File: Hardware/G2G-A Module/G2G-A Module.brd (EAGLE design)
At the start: 13.1 x 12.8 mm, 4 parts, among them J1 GROVE-4P-2.0-3470130P1

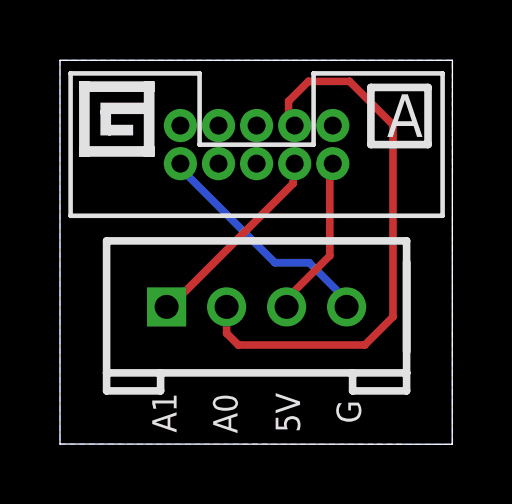
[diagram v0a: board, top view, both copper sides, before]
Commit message: Rotated the G plug 180 degrees.
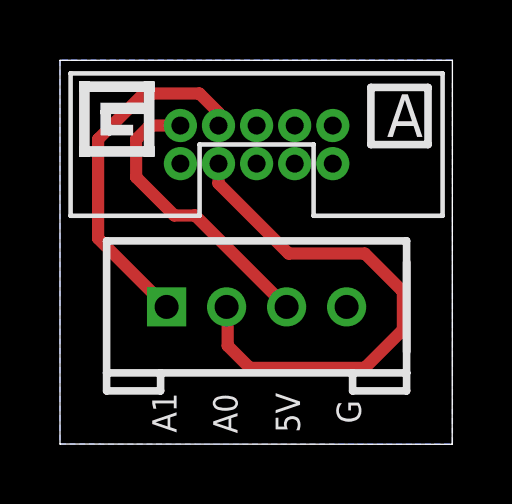
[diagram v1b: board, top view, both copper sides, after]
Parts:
- turned U$1 to 180 degrees
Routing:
- net GND: track 7.74 -> 0.00 mm
- net A1: track 6.59 -> 11.9 mm
- net +5V: track 5.39 -> 9.73 mm
- net A0: track 18.6 -> 17.6 mm
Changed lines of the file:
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@@
 <element name="J1" library="SoftDust" package="4P-2.0" value="GROVE-4P-2.0-3470130P1" x="6.5532" y="4.572" smashed="yes"/>
 <element name="LOGO1" library="SparkFun-Aesthetics" package="OSHW-LOGO-S" value="OSHW-LOGOS" x="1.8796" y="1.778" rot="MR0"/>
-<element name="U$1" library="SoftDust" package="2X5_1.27MM_FEMALE_PLUG" value="2X5_1.27MM_FEMALE_PLUG" x="6.5532" y="9.9822" rot="MR0"/>
+<element name="U$1" library="SoftDust" package="2X5_1.27MM_FEMALE_PLUG" value="2X5_1.27MM_FEMALE_PLUG" x="6.5532" y="9.9822" rot="MR180"/>
 <element name="FRAME1" library="SparkFun-Aesthetics" package="DUMMY" value="" x="0" y="-1.27">
 <attribute name="VERSION" value="v1.0" x="0" y="-1.27" size="1.778" layer="27" display="off"/>
@@
 <contactref element="U$1" pad="10"/>
 <contactref element="J1" pad="4"/>
-<wire x1="4.191" y1="9.017" x2="4.191" y2="9.2456" width="0.254" layer="16"/>
-<wire x1="7.1628" y1="6.0452" x2="4.191" y2="9.017" width="0.254" layer="16"/>
-<wire x1="8.3058" y1="6.0452" x2="7.1628" y2="6.0452" width="0.254" layer="16"/>
-<wire x1="9.4488" y1="4.9022" x2="8.3058" y2="6.0452" width="0.254" layer="16"/>
-<wire x1="4.191" y1="9.2456" x2="4.0132" y2="9.3472" width="0.254" layer="16"/>
-<wire x1="9.4488" y1="4.9022" x2="9.5532" y2="4.572" width="0.254" layer="16"/>
 <polygon width="0.254" layer="16" isolate="0.4064">
 <vertex x="0" y="0"/>
@@
 <contactref element="J1" pad="3"/>
 <contactref element="U$1" pad="2"/>
-<wire x1="8.9916" y1="6.2738" x2="8.9916" y2="9.2456" width="0.254" layer="1"/>
-<wire x1="7.62" y1="4.9022" x2="8.9916" y2="6.2738" width="0.254" layer="1"/>
-<wire x1="8.9916" y1="9.2456" x2="9.0932" y2="9.3472" width="0.254" layer="1"/>
-<wire x1="7.62" y1="4.9022" x2="7.5532" y2="4.572" width="0.254" layer="1"/>
+<wire x1="7.5532" y1="4.572" x2="4.5052" y2="7.62" width="0.4064" layer="1"/>
+<wire x1="4.5052" y1="7.62" x2="3.81" y2="7.62" width="0.4064" layer="1"/>
+<wire x1="3.81" y1="7.62" x2="2.54" y2="8.89" width="0.4064" layer="1"/>
+<wire x1="2.54" y1="8.89" x2="2.54" y2="10.16" width="0.4064" layer="1"/>
+<wire x1="2.54" y1="10.16" x2="2.9972" y2="10.6172" width="0.4064" layer="1"/>
+<wire x1="2.9972" y1="10.6172" x2="4.0132" y2="10.6172" width="0.4064" layer="1"/>
 </signal>
 <signal name="A0">
 <contactref element="J1" pad="2"/>
 <contactref element="U$1" pad="3"/>
-<wire x1="5.5532" y1="4.572" x2="5.5532" y2="3.6924" width="0.254" layer="1"/>
-<wire x1="5.5532" y1="3.6924" x2="5.9436" y2="3.302" width="0.254" layer="1"/>
-<wire x1="5.9436" y1="3.302" x2="10.16" y2="3.302" width="0.254" layer="1"/>
-<wire x1="10.16" y1="3.302" x2="11.0998" y2="4.2418" width="0.254" layer="1"/>
-<wire x1="11.0998" y1="4.2418" x2="11.0998" y2="10.6426" width="0.254" layer="1"/>
-<wire x1="11.0998" y1="10.6426" x2="9.652" y2="12.0904" width="0.254" layer="1"/>
-<wire x1="9.652" y1="12.0904" x2="8.2804" y2="12.0904" width="0.254" layer="1"/>
-<wire x1="8.2804" y1="12.0904" x2="7.62" y2="11.43" width="0.254" layer="1"/>
-<wire x1="7.62" y1="11.43" x2="7.62" y2="10.8204" width="0.254" layer="1"/>
-<wire x1="7.62" y1="10.8204" x2="7.8232" y2="10.6172" width="0.254" layer="1"/>
+<wire x1="5.5532" y1="4.572" x2="5.588" y2="4.5372" width="0.4064" layer="1"/>
+<wire x1="5.588" y1="4.5372" x2="5.588" y2="3.2766" width="0.4064" layer="1"/>
+<wire x1="5.588" y1="3.2766" x2="6.3246" y2="2.54" width="0.4064" layer="1"/>
+<wire x1="6.3246" y1="2.54" x2="10.16" y2="2.54" width="0.4064" layer="1"/>
+<wire x1="10.16" y1="2.54" x2="11.43" y2="3.81" width="0.4064" layer="1"/>
+<wire x1="11.43" y1="3.81" x2="11.43" y2="5.08" width="0.4064" layer="1"/>
+<wire x1="11.43" y1="5.08" x2="10.16" y2="6.35" width="0.4064" layer="1"/>
+<wire x1="10.16" y1="6.35" x2="7.62" y2="6.35" width="0.4064" layer="1"/>
+<wire x1="7.62" y1="6.35" x2="5.2832" y2="8.6868" width="0.4064" layer="1"/>
+<wire x1="5.2832" y1="8.6868" x2="5.2832" y2="9.3472" width="0.4064" layer="1"/>
 </signal>
 <signal name="A1">
 <contactref element="J1" pad="1"/>
 <contactref element="U$1" pad="4"/>
-<wire x1="7.7724" y1="8.6868" x2="7.7724" y2="9.144" width="0.254" layer="1"/>
-<wire x1="3.6576" y1="4.572" x2="7.7724" y2="8.6868" width="0.254" layer="1"/>
-<wire x1="7.7724" y1="9.144" x2="7.8232" y2="9.3472" width="0.254" layer="1"/>
-<wire x1="3.6576" y1="4.572" x2="3.5532" y2="4.572" width="0.254" layer="1"/>
+<wire x1="3.5532" y1="4.572" x2="1.27" y2="6.8552" width="0.4064" layer="1"/>
+<wire x1="1.27" y1="6.8552" x2="1.27" y2="10.16" width="0.4064" layer="1"/>
+<wire x1="1.27" y1="10.16" x2="2.794" y2="11.684" width="0.4064" layer="1"/>
+<wire x1="2.794" y1="11.684" x2="4.6482" y2="11.684" width="0.4064" layer="1"/>
+<wire x1="4.6482" y1="11.684" x2="5.2832" y2="11.049" width="0.4064" layer="1"/>
+<wire x1="5.2832" y1="11.049" x2="5.2832" y2="10.6172" width="0.4064" layer="1"/>
 </signal>
 </signals>

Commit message: Replaced all 'G' logos with a new part for the logo.
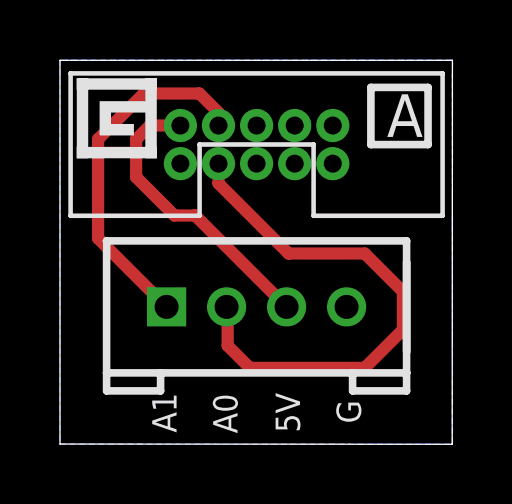
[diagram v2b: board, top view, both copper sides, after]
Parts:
- added U$2: GADGETEER_LOGO_SMALL, SoftDust:GADGETEER_LOGO_SMALL
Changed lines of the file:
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@@
 <setting verticaltext="up"/>
 </settings>
-<grid distance="0.05" unitdist="inch" unit="mm" style="lines" multiple="1" display="no" altdistance="0.0254" altunitdist="mm" altunit="mm"/>
+<grid distance="1.27" unitdist="mm" unit="mm" style="lines" multiple="1" display="yes" altdistance="0.0254" altunitdist="mm" altunit="mm"/>
 <layers>
 <layer number="1" name="Top" color="4" fill="1" visible="yes" active="yes"/>
@@
 <text x="5.9182" y="0.3556" size="0.8128" layer="21" font="vector" rot="R90">A0</text>
 <text x="3.8862" y="0.381" size="0.8128" layer="21" font="vector" rot="R90">A1</text>
-<rectangle x1="0.635" y1="9.5758" x2="3.1496" y2="9.9314" layer="21"/>
-<rectangle x1="0.635" y1="11.7348" x2="3.1496" y2="12.0904" layer="21"/>
-<rectangle x1="1.7145" y1="10.6553" x2="4.2291" y2="11.0109" layer="21" rot="R90"/>
-<rectangle x1="-0.4445" y1="10.6553" x2="2.0701" y2="11.0109" layer="21" rot="R90"/>
-<rectangle x1="1.3462" y1="10.9982" x2="2.8194" y2="11.3792" layer="21"/>
-<rectangle x1="1.3462" y1="10.287" x2="1.7018" y2="11.1252" layer="21"/>
-<rectangle x1="1.8415" y1="10.0457" x2="2.1971" y2="10.8839" layer="21" rot="R90"/>
 </plain>
 <attributes>
@@
 <attribute name="DESIGNER" value="Ian Lee" x="0" y="-1.27" size="1.778" layer="27" display="off"/>
 </element>
+<element name="U$2" library="SoftDust" package="GADGETEER_LOGO_SMALL" value="GADGETEER_LOGO_SMALL" x="0.5588" y="9.525"/>
 </elements>
 <signals>
